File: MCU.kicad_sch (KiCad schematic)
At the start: 37 parts, among them J10 Conn_01x12, J2 USB_C_Receptacle_USB2.0, J8 Conn_01x04, Q3 AO3400A, SW2 BUTTON, SW2 RESET, U4 STM32F405RGTx, Y1 16MHz

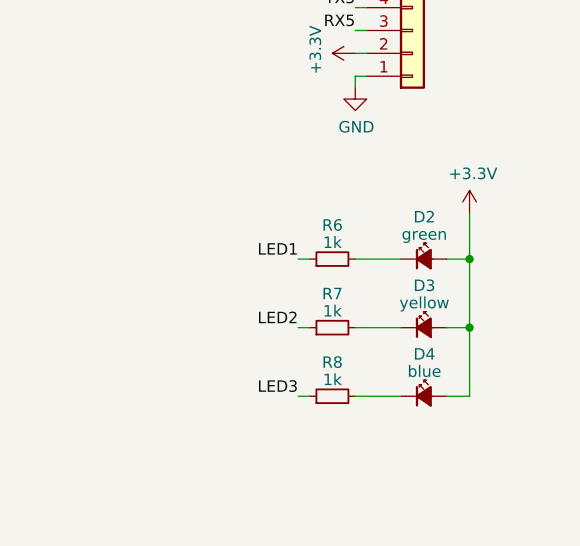
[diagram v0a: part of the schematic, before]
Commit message: improved sensor design
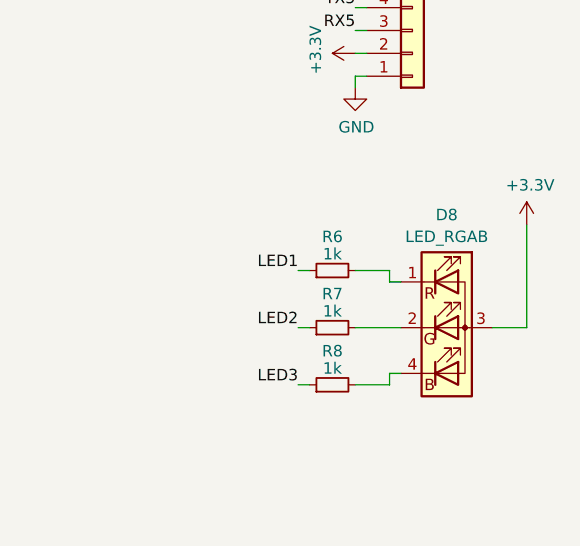
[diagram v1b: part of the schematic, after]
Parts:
- removed D2: green, LED_SMD:LED_0603_1608Metric, symbol Device:LED_Small_Filled
- removed D3: yellow, LED_SMD:LED_0603_1608Metric, symbol Device:LED_Small_Filled
- removed D4: blue, LED_SMD:LED_0603_1608Metric, symbol Device:LED_Small_Filled
- added D8: LED_RGAB, LED_SMD:LED_RGB_1210, symbol Device:LED_RGAB
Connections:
- net +3V3: now also D8.3 (A)
- net at R7.2: now also D8.2 (GK)
- net at R6.2: now also D8.1 (RK)
- net at R8.2: now also D8.4 (BK)
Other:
- moved on the sheet: R6, R8
